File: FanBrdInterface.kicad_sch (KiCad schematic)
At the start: 14 parts

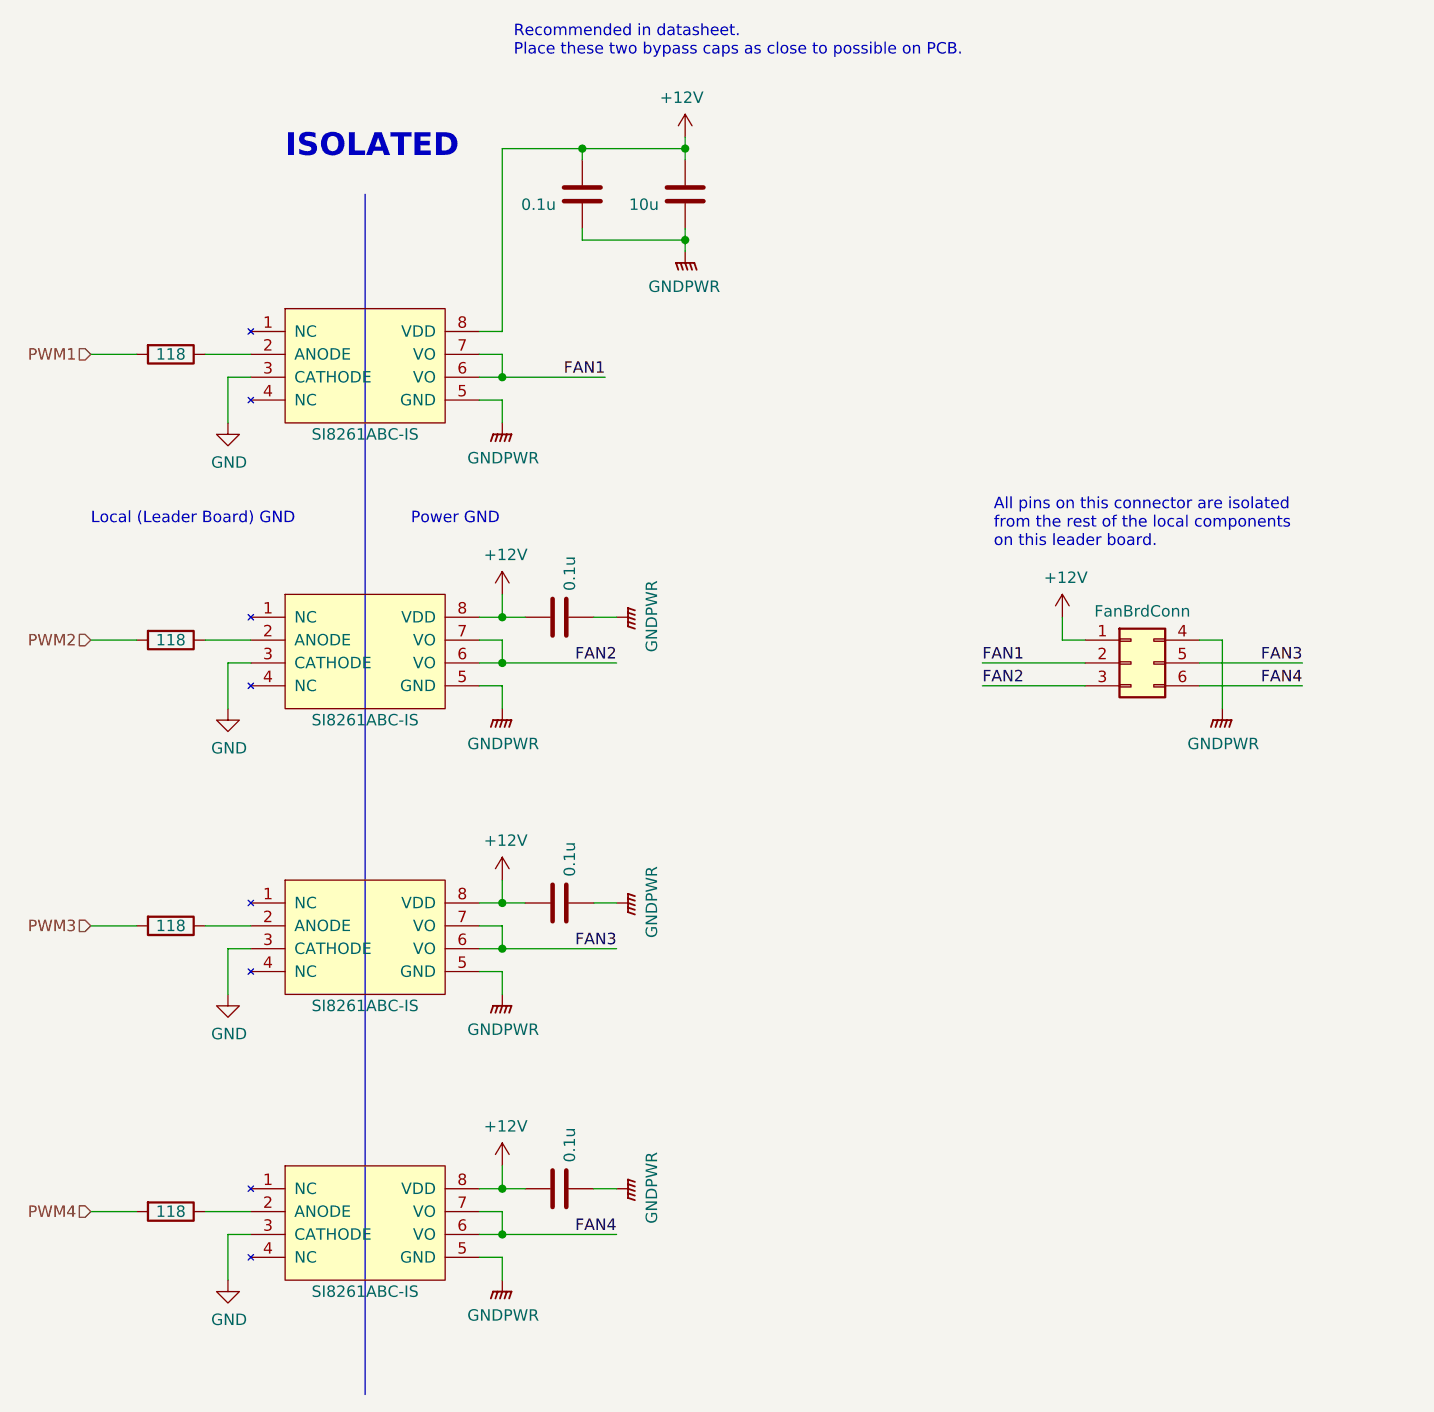
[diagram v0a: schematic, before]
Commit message: Update repo to only use one common library
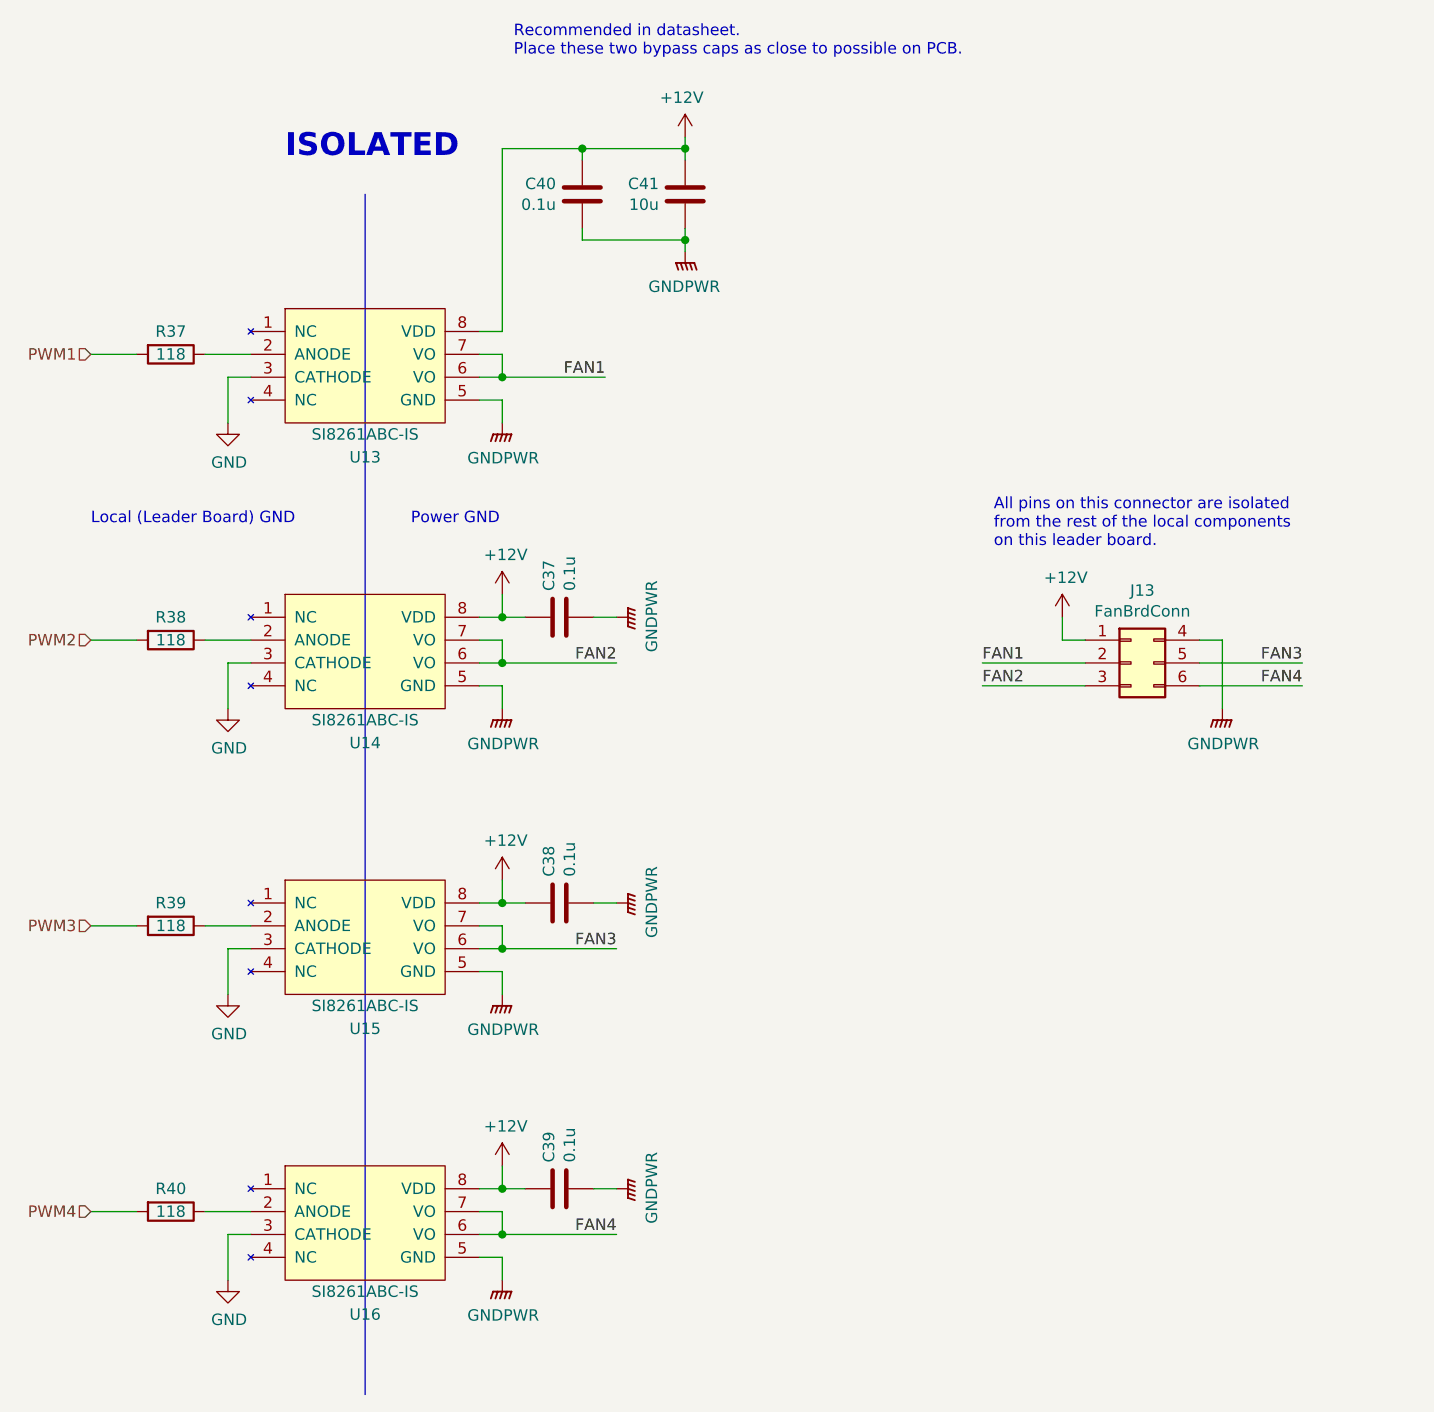
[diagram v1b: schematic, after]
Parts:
- gave numbers to parts that had none: 14
